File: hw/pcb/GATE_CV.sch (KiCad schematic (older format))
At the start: 34 parts, among them J601 CV0IN, J602 TRG0, J603 CV1IN, J604 TRG1, Q601 SS8050, Q602 SS8050, SW601 SW_Push_Dual, SW602 SW_Push_Dual, U601 MCP6002-xSN

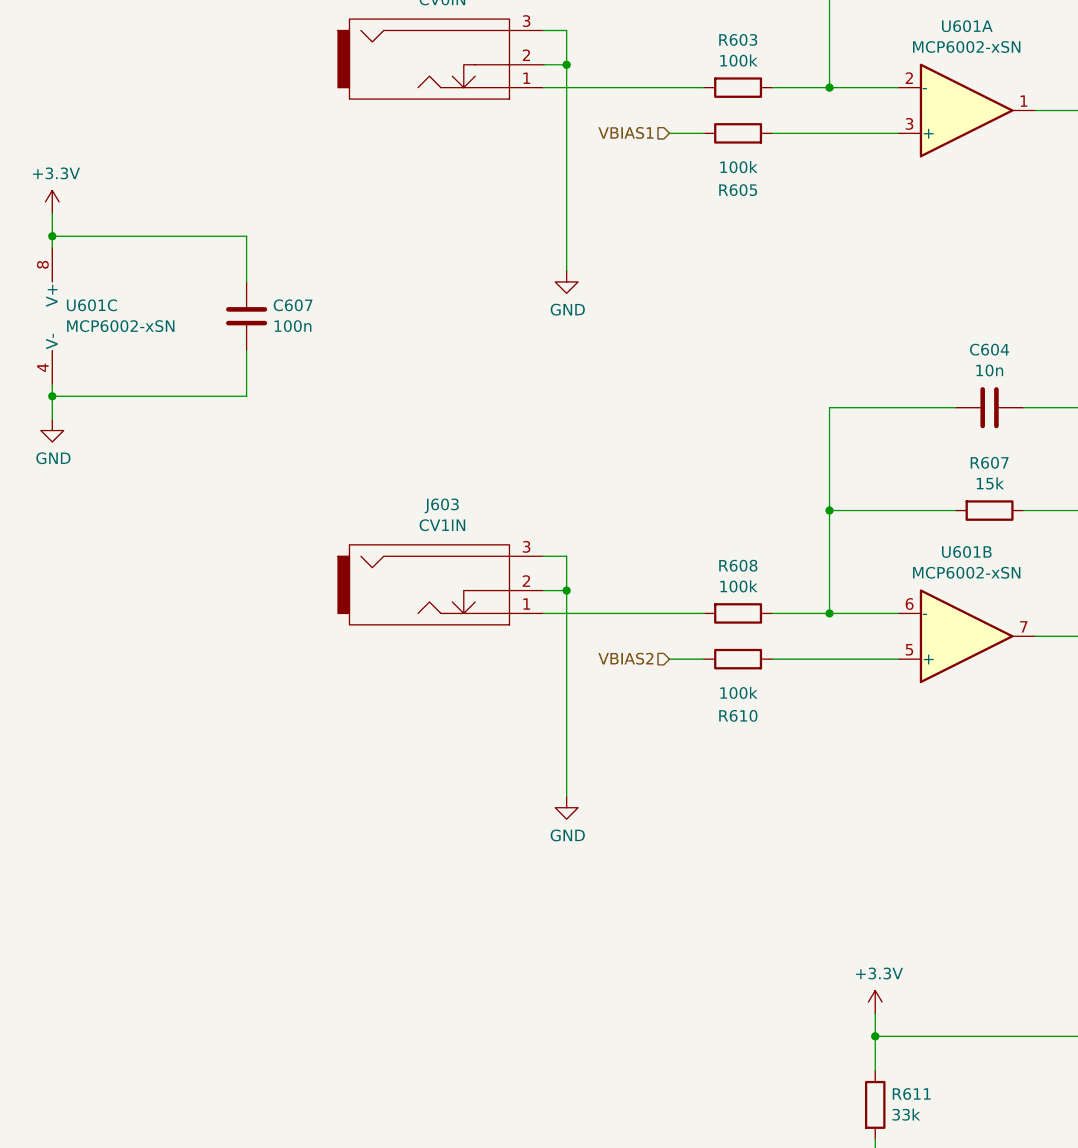
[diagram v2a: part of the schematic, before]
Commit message: Updated Eurorack hw to Rev. H
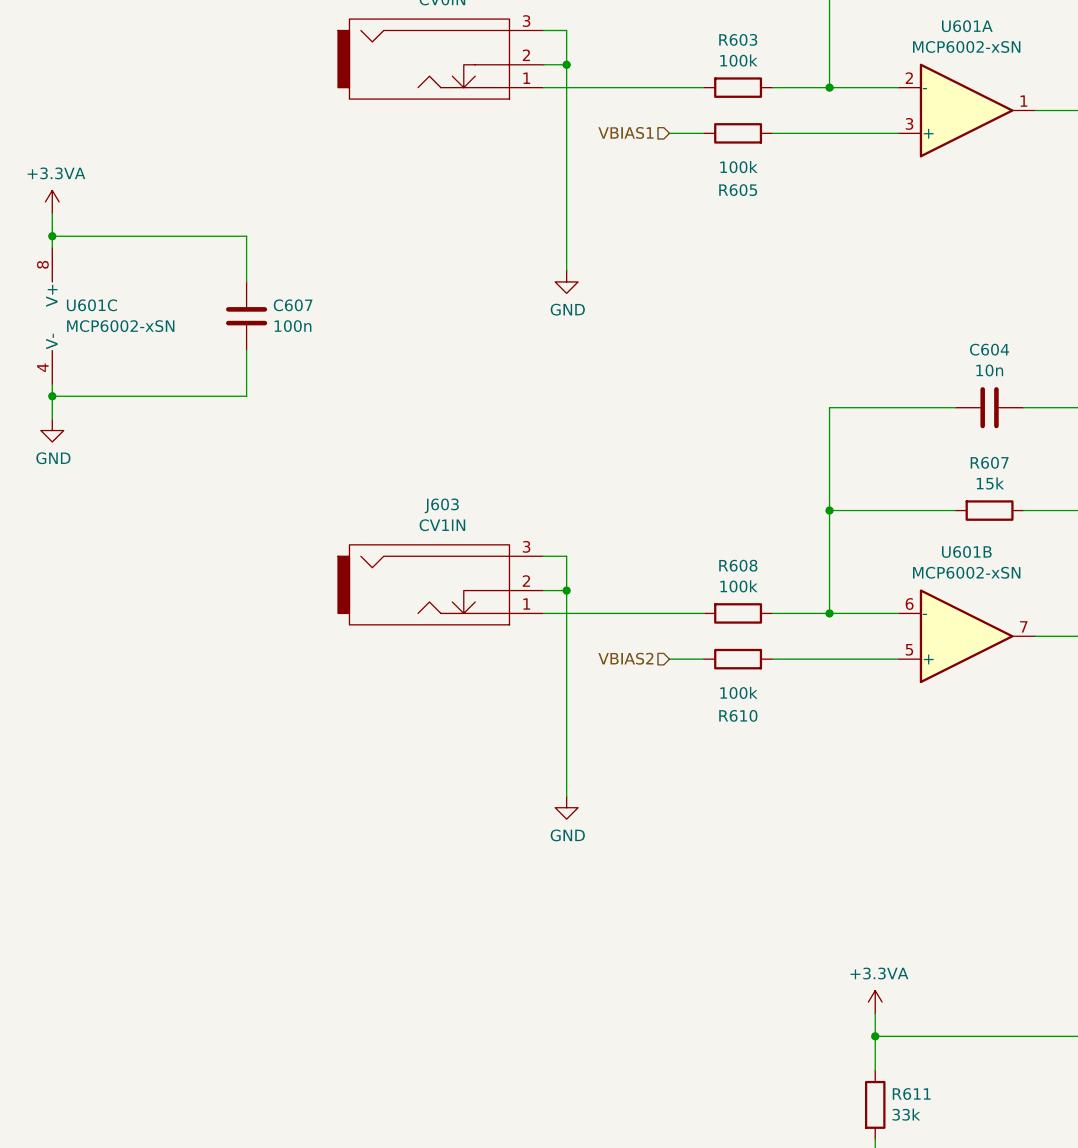
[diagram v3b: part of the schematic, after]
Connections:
- net +3V3: no longer C607.1, R611.1, R612.1, U601.8 (V+)
- new net +3.3VA: C607.1, R611.1, R612.1, U601.8 (V+)
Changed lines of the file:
@@
 Sheet 6 6
 Title "ESP32 Eurorack Audio Module"
-Date "2020-08-18"
-Rev "G"
-Comp "(c) Robert Manzke 2020"
+Date "2021-10-05"
+Rev "H"
+Comp "(c) Robert Manzke 2021"
 Comment1 "https://creativecommons.org/licenses/by-nc-sa/4.0/"
 Comment2 "Licensed under CC BY-NC-SA 4.0"
@@
 Wire Wire Line
 	1550 4500 1550 4550
-$Comp
-L power:+3.3V #PWR0613
-U 1 1 5DBF03A4
-P 1550 3750
-F 0 "#PWR0613" H 1550 3600 50  0001 C CNN
-F 1 "+3.3V" H 1565 3923 50  0000 C CNN
-F 2 "" H 1550 3750 50  0001 C CNN
-F 3 "" H 1550 3750 50  0001 C CNN
-	1    1550 3750
-	1    0    0    -1
-$EndComp
 Wire Wire Line
 	1550 3750 1550 3850
@@
 NoConn ~ 12200 5300
 NoConn ~ 12200 5500
-$Comp
-L power:+3.3V #PWR0102
-U 1 1 5DD0C81D
-P 5150 7250
-F 0 "#PWR0102" H 5150 7100 50  0001 C CNN
-F 1 "+3.3V" H 5165 7423 50  0000 C CNN
-F 2 "" H 5150 7250 50  0001 C CNN
-F 3 "" H 5150 7250 50  0001 C CNN
-	1    5150 7250
-	1    0    0    -1
-$EndComp
 Text HLabel 4250 3400 0    50   Input ~ 0
 VBIAS1
@@
 	5150 7250 5150 7350
 Connection ~ 5150 7350
+$Comp
+L power:+3.3VA #PWR0102
+U 1 1 615E7F53
+P 1550 3750
+F 0 "#PWR0102" H 1550 3600 50  0001 C CNN
+F 1 "+3.3VA" H 1565 3923 50  0000 C CNN
+F 2 "" H 1550 3750 50  0001 C CNN
+F 3 "" H 1550 3750 50  0001 C CNN
+	1    1550 3750
+	1    0    0    -1
+$EndComp
+$Comp
+L power:+3.3VA #PWR0103
+U 1 1 615E968D
+P 5150 7250
+F 0 "#PWR0103" H 5150 7100 50  0001 C CNN
+F 1 "+3.3VA" H 5165 7423 50  0000 C CNN
+F 2 "" H 5150 7250 50  0001 C CNN
+F 3 "" H 5150 7250 50  0001 C CNN
+	1    5150 7250
+	1    0    0    -1
+$EndComp
 $EndSCHEMATC
